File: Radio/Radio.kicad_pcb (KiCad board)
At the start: 2 copper layers, 89.7 x 83 mm, 26 parts, among them J1 CUE_SJ1-352XNG, SW1 Bourns PEC11R, SW2 Bourns PEC11R, SW3 SW_Push, SW4 SW_Push, SW5 SW_Push, SW6 SW_Push, U1 LM386, U2 RDA5807M_Module, U3 LM386

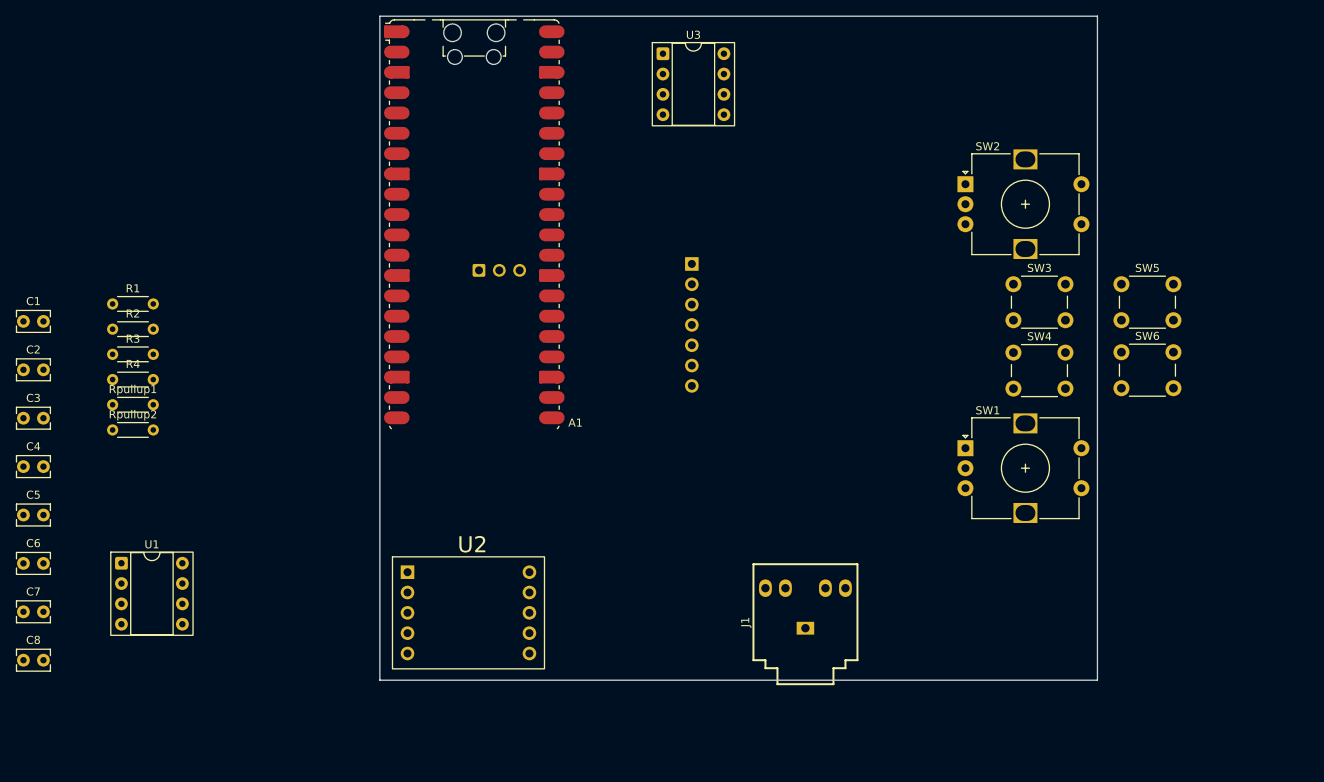
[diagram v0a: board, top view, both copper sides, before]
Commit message: Finished making first version of the pcb design. Added fornt and back copper and filled the back with copper. Also removed one of the two amplifiers.
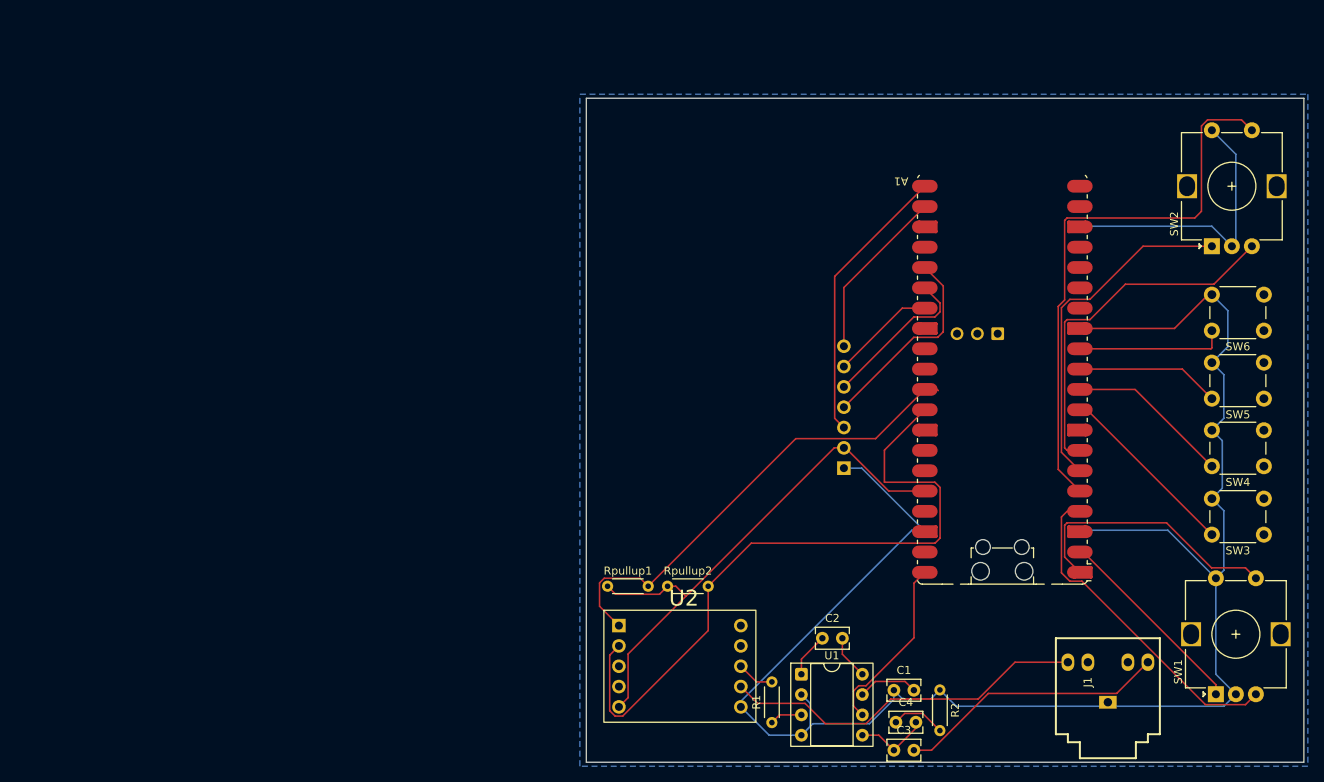
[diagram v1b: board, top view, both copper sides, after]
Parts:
- removed C5: C_US, Capacitor_THT:C_Rect_L4.0mm_W2.5mm_P2.50mm
- removed C6: 10uF, Capacitor_THT:C_Rect_L4.0mm_W2.5mm_P2.50mm
- removed C7: 0.05uF, Capacitor_THT:C_Rect_L4.0mm_W2.5mm_P2.50mm
- removed C8: 250uF, Capacitor_THT:C_Rect_L4.0mm_W2.5mm_P2.50mm
- removed the R2 at (38.9, 75.6)
- removed R3: 10, Resistor_THT:R_Axial_DIN0204_L3.6mm_D1.6mm_P5.08mm_Horizontal
- removed U3: LM386, Package_DIP:DIP-8_W7.62mm_Socket
- C3: value 250uF -> 470uF
- moved C1 118.2 mm to (136.6, 120.8)
- moved C3 116.5 mm to (136.6, 128.3)
- moved C4 113.6 mm to (136.8, 124.8)
- moved R2 110.4 mm to (142.3, 120.7), turned to -90 degrees
- moved C2 105.4 mm to (127.6, 114.3)
- moved R1 97.6 mm to (121.3, 124.8), turned to 90 degrees
- moved U1 86.1 mm to (125.0, 118.8)
- moved Rpullup2 72.1 mm to (108.3, 107.8)
- moved A1 68.8 mm to (150.1, 81.9), turned to 180 degrees
- moved Rpullup1 65.9 mm to (100.8, 107.8)
- moved DISP1 64.1 mm to (98.4, 103.1), turned to 90 degrees
- moved SW3 44.3 mm to (182.8, 101.3), turned to 180 degrees
- moved SW1 43.9 mm to (176.8, 121.3), turned to 90 degrees
- moved J1 38.9 mm to (163.3, 122.3)
- moved SW4 34.4 mm to (182.8, 92.8), turned to 180 degrees
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- renumbered R4 to R2
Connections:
- A1 pad 10: Net-(A1-GPIO6) -> Net-(A1-GPIO7)
- A1 pad 11: Net-(A1-GPIO6) -> Net-(A1-GPIO8)
- A1 pad 12: Net-(A1-GPIO6) -> Net-(A1-GPIO9)
- J1 pad 2: Net-(C8-Pad2) -> Net-(U2-ROUT)
- SW4 pad 1: Net-(A1-GPIO6) -> Net-(A1-GPIO7)
- SW5 pad 1: Net-(A1-GPIO6) -> Net-(A1-GPIO8)
- SW6 pad 1: Net-(A1-GPIO6) -> Net-(A1-GPIO9)
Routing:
- net Net-(DISP1-VSS/GND): track 0.00 -> 250.6 mm
- net Net-(A1-GPIO27_ADC1): track 0.00 -> 87.3 mm
- net Net-(A1-GPIO3): track 0.00 -> 70.7 mm
- net Net-(A1-3V3): track 0.00 -> 68.2 mm
- net Net-(A1-GPIO26_ADC0): track 0.00 -> 58.1 mm
- net Net-(U2-ROUT): track 0.00 -> 46.0 mm
- net Net-(A1-GPIO5): track 0.00 -> 45.1 mm
- net Net-(A1-GPIO4): track 0.00 -> 43.3 mm
- net Net-(A1-GPIO2): track 0.00 -> 41.2 mm
- net Net-(A1-GPIO16): track 0.00 -> 35.3 mm
- net Net-(C3-Pad2): track 0.00 -> 33.8 mm
- net Net-(A1-GPIO0): track 0.00 -> 33.6 mm
- net Net-(A1-GPIO19): track 0.00 -> 25.3 mm
- net Net-(A1-GPIO1): track 0.00 -> 25.1 mm
- net Net-(A1-GPIO6): track 0.00 -> 23.0 mm
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- added copper zone on B.Cu, net Net-(DISP1-VSS/GND)

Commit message: Add files via upload
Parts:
- removed J1: CUE_SJ1-352XNG, ECE:CUE_SJ1-352XNG
- removed SW5, SW6: SW_Push, Button_Switch_THT:SW_PUSH_6mm
- added LS1: Speaker, Buzzer_Beeper:Speaker_CUI_CMR-1206S-67, F.Cu at (164.0, 126.0)
- moved SW4 12.5 mm to (182.8, 80.2)
- moved SW3 7.06 mm to (182.8, 94.2)
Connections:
- A1 pad 11: Net-(A1-GPIO8) -> unconnected-(A1-GPIO8-Pad11)
- A1 pad 12: Net-(A1-GPIO9) -> unconnected-(A1-GPIO9-Pad12)
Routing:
- net Net-(DISP1-VSS/GND): track 250.6 -> 218.1 mm
- net Net-(A1-GPIO9): track 18.7 -> 0.00 mm
- net Net-(A1-GPIO8): track 18.0 -> 0.00 mm
- net Net-(A1-GPIO6): track 23.0 -> 20.0 mm
- net Net-(U2-ROUT): track 46.0 -> 44.2 mm
- net Net-(C3-Pad2): track 33.8 -> 32.2 mm
- net Net-(A1-GPIO7): track 20.5 -> 19.8 mm
